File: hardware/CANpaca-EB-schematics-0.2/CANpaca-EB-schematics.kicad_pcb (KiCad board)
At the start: 4 copper layers, 42 x 42 mm, 132 parts, among them J11 Conn_01x03_Male, J12 A2501WV-4P, J13 A2501WV-3P, J14 A2501WV-5P, J16 A2501WV-3P, J17 A2501WV-2P, J2 FAN_0, J4 Conn_01x03_Male, J5 FAN_1, J6 Screw_Terminal_01x02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

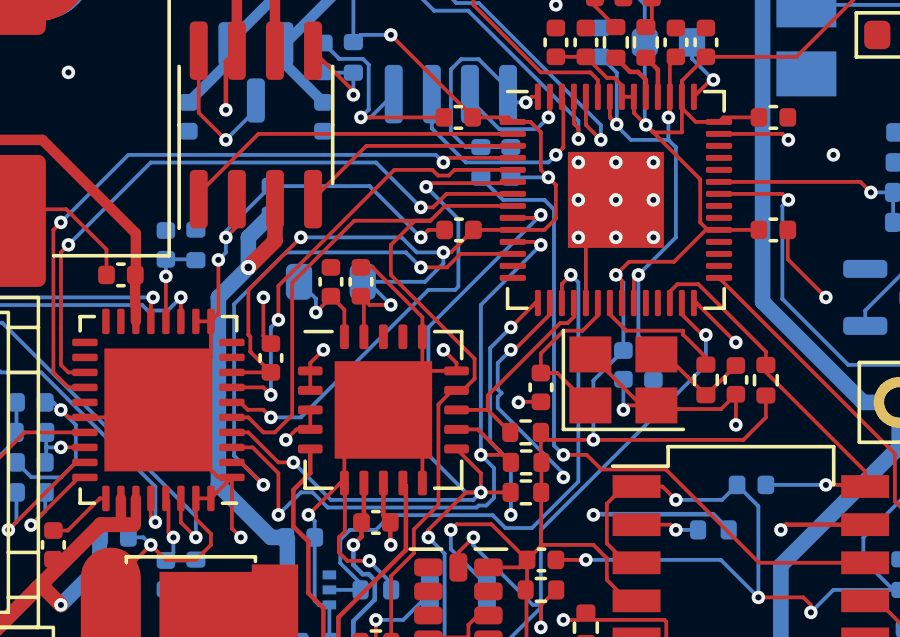
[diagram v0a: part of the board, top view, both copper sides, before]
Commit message: changed to hardware spi
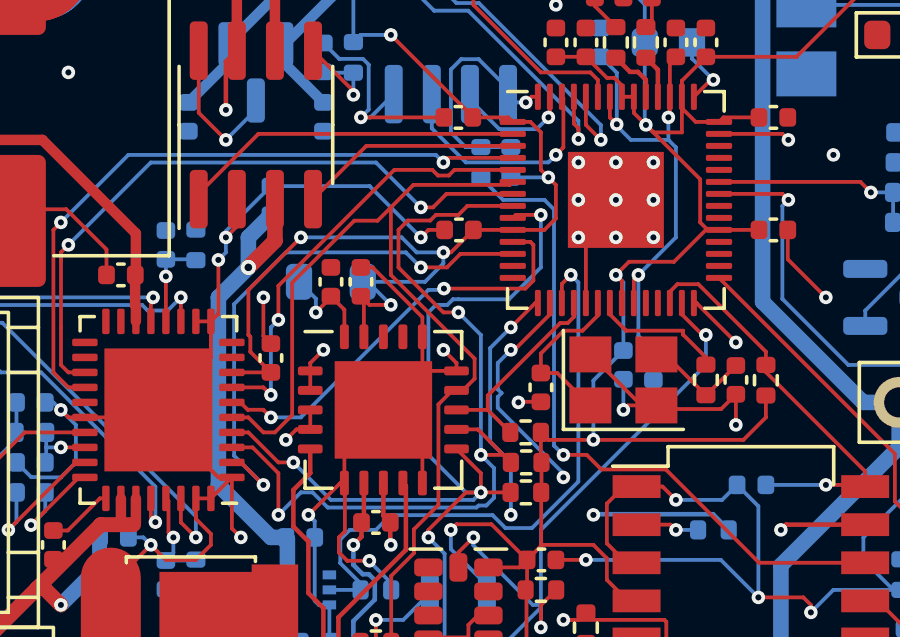
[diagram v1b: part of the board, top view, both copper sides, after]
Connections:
- U10 pad 11: SCK -> STEP_E
- U10 pad 6: STEP_E -> MISO
- U10 pad 8: MISO -> SCK
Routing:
- net SCK: track 39.2 -> 43.5 mm
- net STEP_E: track 16.3 -> 14.1 mm
- net MOSI: track 32.0 -> 33.3 mm
